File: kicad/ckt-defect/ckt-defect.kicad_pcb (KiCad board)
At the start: 2 copper layers, 99.1 x 61 mm, 73 parts, among them J1 Screw_Terminal_01x02, J10 Micro_SD_Card_Det_Hirose_DM3AT, J11 690-005-299-043, J12 SM04B-SRSS, J13 Conn_01x03, J14 Conn_01x03, J2 SM04B-SRSS, J3 SM04B-SRSS, J4 SM04B-SRSS, J5 SM04B-SRSS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

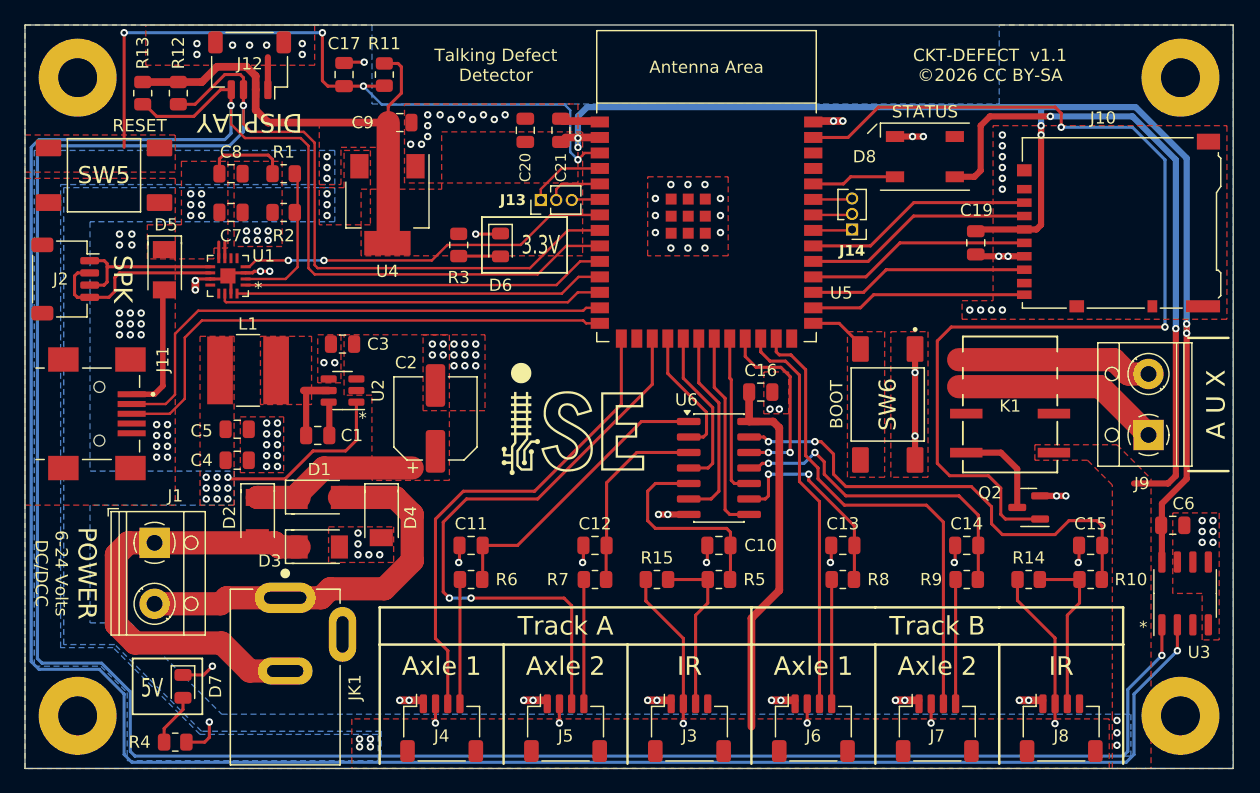
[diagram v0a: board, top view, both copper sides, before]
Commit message: Improved buffering
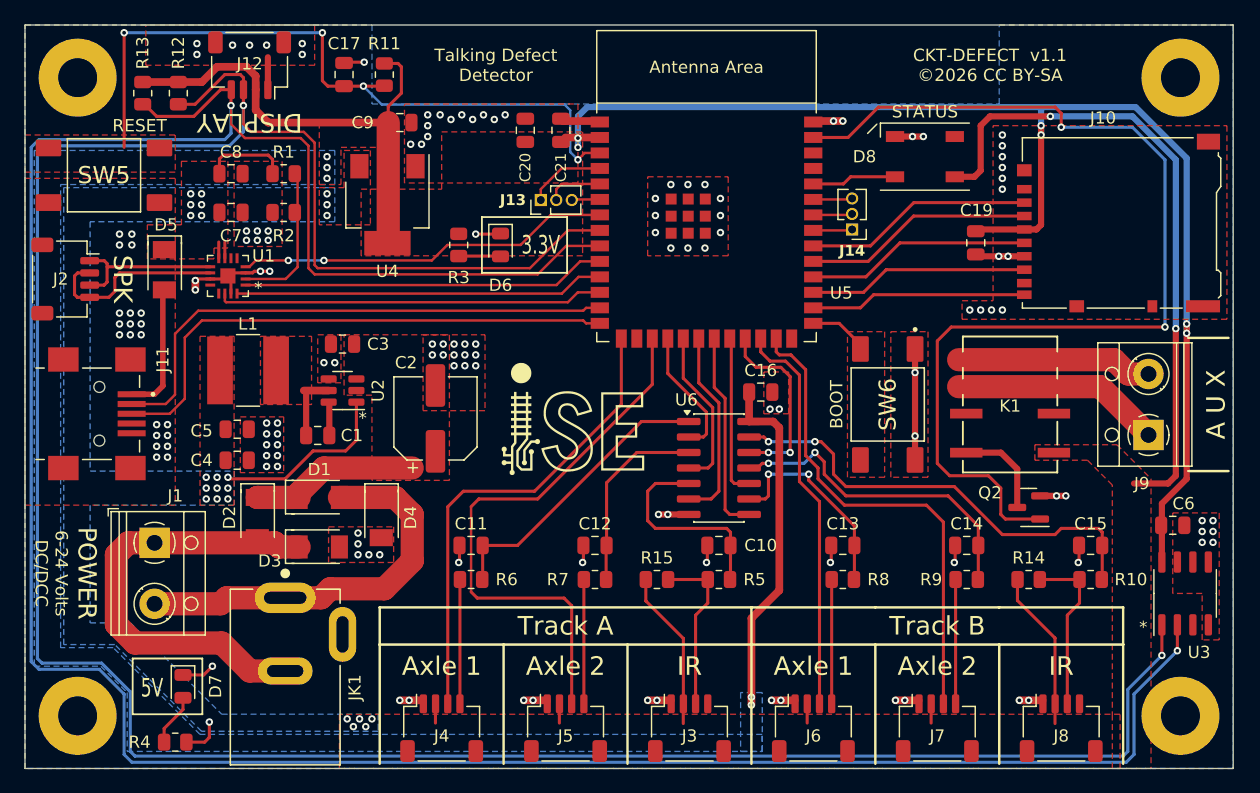
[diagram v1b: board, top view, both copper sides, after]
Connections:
- J3 pad MP: +3.3V -> +5V
- J4 pad MP: +3.3V -> +5V
- J5 pad MP: +3.3V -> +5V
- J6 pad MP: +3.3V -> +5V
- J7 pad MP: +3.3V -> +5V
- J8 pad MP: +3.3V -> +5V
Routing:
- net /AXLE_A2_EN: track 50.3 -> 46.5 mm, vias 2 -> 0
- net +3.3V: track 179.3 -> 177.5 mm, vias 13 -> 11
- net /TRKB_int: track 39.1 -> 37.5 mm
- net /AXLE_A1_EN: track 40.1 -> 39.3 mm
- net /AXLE_B2_int: track 26.6 -> 26.1 mm
- net +5V: vias 30 -> 26

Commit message: Changed to Kicad footprint for QFN
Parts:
- U1: footprint ISE_UltraLibrarian:21-0136I_T1633-4_MXM -> Package_DFN_QFN:TQFN-16-1EP_3x3mm_P0.5mm_EP1.23x1.23mm
